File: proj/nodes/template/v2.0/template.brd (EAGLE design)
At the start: 9 parts, among them J1 54602-908LF, U1 LM2674MX-5.0/NOPB

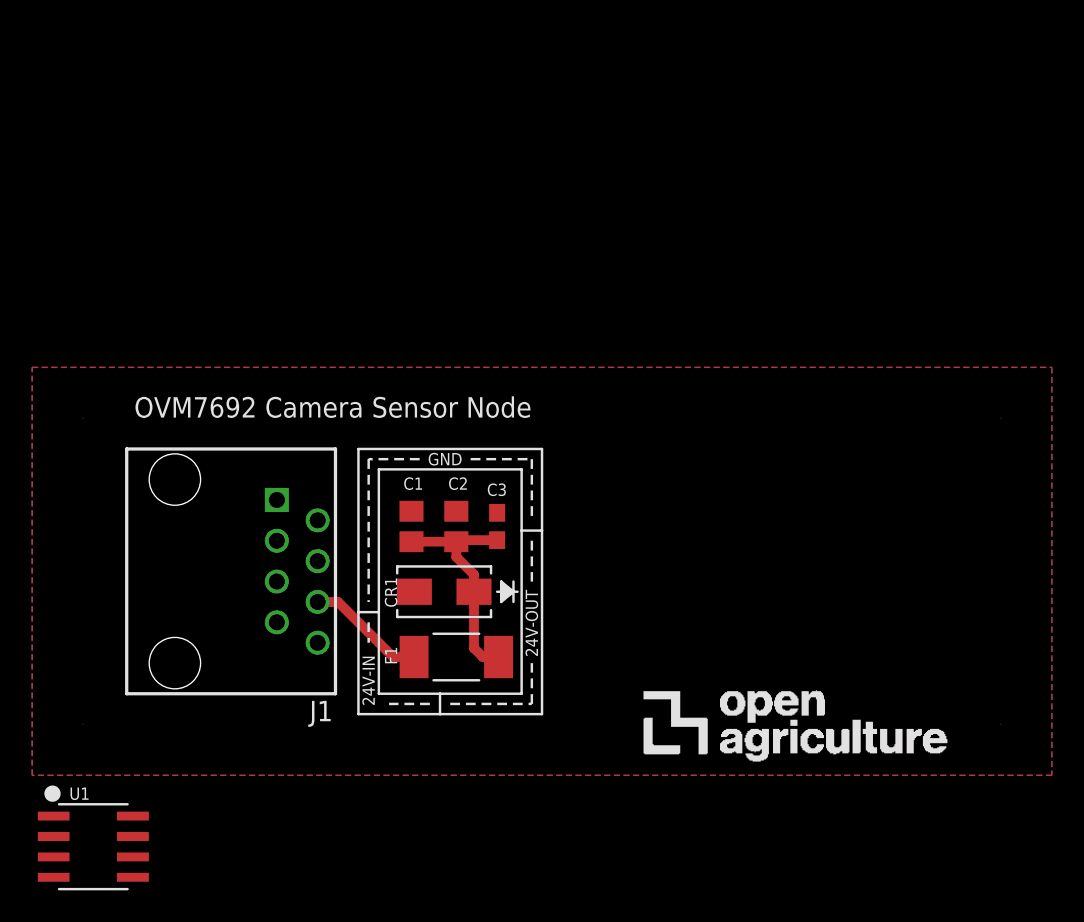
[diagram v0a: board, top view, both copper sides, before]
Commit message: added hotkey config and 5v switching regulator
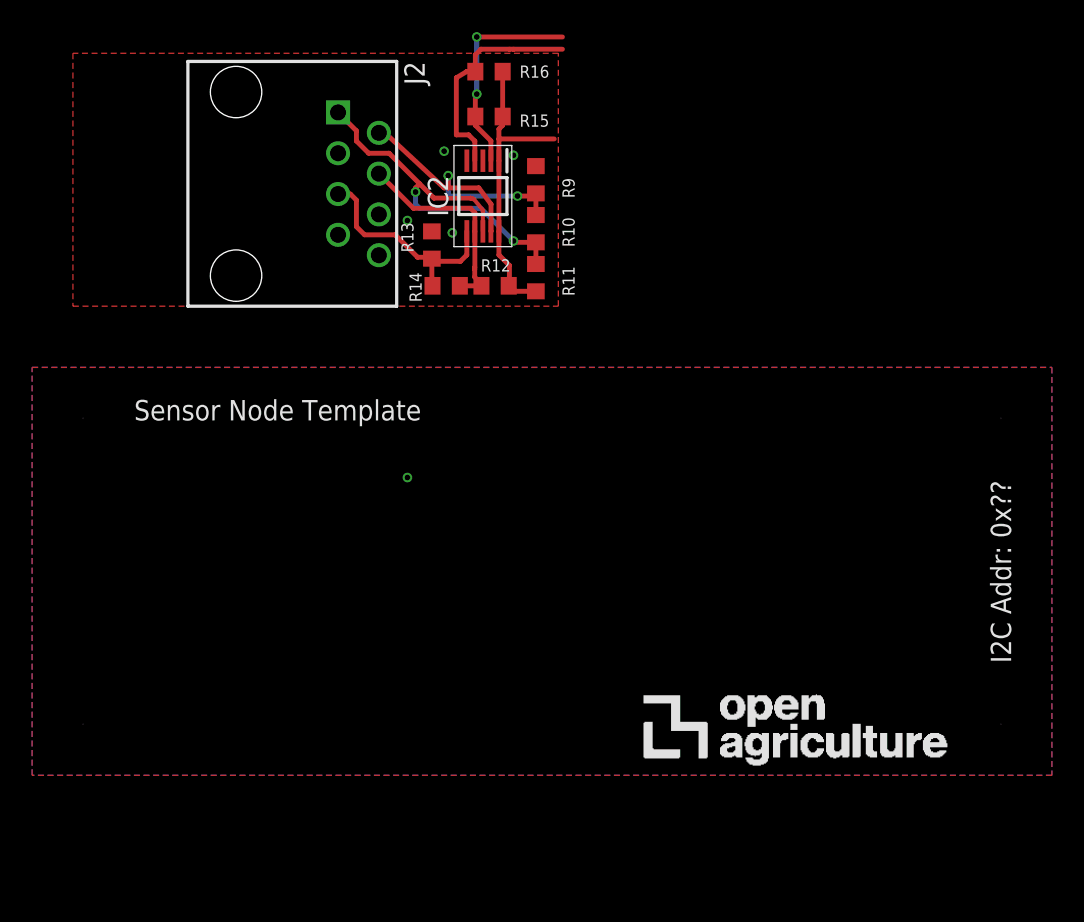
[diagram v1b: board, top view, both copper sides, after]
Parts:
- removed C1: 10uF, openag-capacitors:C0805
- removed C2: 4.7uF, openag-capacitors:C0805
- removed C3: 0.1uF, openag-capacitors:C0603
- removed CR1: SMAJ26A-13-F, openag-diodes:SMA
- removed F1: SST 7, openag-fuses:SS
- removed J1: 54602-908LF, openag-connectors:OPENAG-V1-RJ45
- removed U$2: (no value), openag-frames:OPENAG-LOGO-750-MIL
- removed U1: LM2674MX-5.0/NOPB, openag-regulators:M08A
- added IC2: PCA9615DP, PCA9615DP:SOP50P490X110-10N
- added J2: 54602-908LF, openag_connector:OPENAG-V1-RJ45
- added R10, R11, R12, R13, R14, R15, R16, R9: (no value), rcl:R0603
- added U$1: (no value), openag-frames:OPENAG-LOGO-750-MIL
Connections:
- removed net 24V_IN: F1.1, J1.24V(6)
- new net +3V3: IC2.1, IC2.10, R11.1, R12.2, R15.2, R16.2
- new net DSCLM: IC2.6, J2.DSCLM(5), R13.2, R14.1
- new net DSCLP: IC2.7, J2.DSCLP(4), R12.1, R14.2
- new net DSDAM: IC2.9, J2.DSDAM(2), R10.2, R9.1
- new net DSDAP: IC2.8, J2.DSDAP(1), R10.1, R11.2
- new net SCL_X: IC2.4, R16.1
- new net SDA_X: IC2.2, R15.1
- new net USBM: J2.USBM(8)
- new net USBP: J2.USBP(7)
- net +24V: now also J2.24V(6); no longer C1.1, C2.1, C3.1, CR1.1, F1.2
- net GND: now also IC2.5, J2.GND(3), R13.1, R9.2; no longer C1.2, C2.2, C3.2, CR1.2, J1.GND(3)
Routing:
- net DSDAP: track 0.00 -> 24.4 mm, vias 0 -> 2
- net DSDAM: track 0.00 -> 19.6 mm, vias 0 -> 2
- net +3V3: track 0.00 -> 19.0 mm
- net +24V: track 14.3 -> 0.00 mm
- net SCL_X: track 0.00 -> 14.0 mm
- net DSCLM: track 0.00 -> 14.0 mm
- net SDA_X: track 0.00 -> 13.5 mm, vias 0 -> 2
- net DSCLP: track 0.00 -> 13.0 mm
- net 24V_IN: track 7.43 -> 0.00 mm
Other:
- board text added: "I2C Addr: 0x??"
- board text added: "Sensor Node Template"
- board text removed: "24V-IN"
- board text removed: "24V-OUT"
- board text removed: "GND"
- board text removed: "OVM7692 Camera Sensor Node"
